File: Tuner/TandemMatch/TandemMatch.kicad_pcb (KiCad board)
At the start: 2 copper layers, 100 x 100 mm, 104 parts, among them J1 Conn_01x02, J10 Conn_01x01, J11 Conn_01x01, J12 Conn_01x01, J13 Conn_01x01, J14 Conn_01x01, J15 Conn_01x01, J16 Conn_01x01, J17 Conn_01x02, J18 Conn_Coaxial, J19 Conn_01x02, J2 Conn_01x02, J20 Conn_Coaxial, J21 Conn_01x01, J22 Conn_01x01, J23 Conn_01x01, J24 Conn_01x01, J25 Conn_01x01, J26 Conn_01x01, J27 Conn_01x01, J28 Conn_01x01, J29 Conn_01x01, J3 Conn_Coaxial, J30 Conn_01x01, J31 Conn_01x01, J32 Conn_01x01, J33 Conn_01x03, J34 Conn_01x01, J35 Conn_01x01, J36 Conn_01x01, J37 Conn_01x01, J38 Conn_01x01, J39 Conn_01x01, J4 Conn_Coaxial, J40 Conn_01x01, J41 Conn_01x01, J42 Conn_Coaxial, J43 Conn_Coaxial, J44 Conn_01x01, J45 Conn_01x01, J46 Conn_01x01, J47 Conn_01x01, J48 Conn_01x01, J49 Conn_01x01, J5 Conn_01x01, J50 Conn_01x01, J51 Conn_01x01, J52 Conn_01x01, J53 Conn_01x01, J54 Conn_01x01, J55 Conn_01x01, J56 Conn_01x01, J57 Conn_01x01, J58 Conn_01x01, J59 Conn_01x01, J6 Conn_01x01, J60 Conn_Coaxial, J61 Conn_Coaxial, J62 Conn_01x04, J63 Conn_01x01, J64 Conn_01x01, J65 Conn_01x01, J66 Conn_01x01, J7 Conn_01x01, J8 Conn_01x01, J9 Conn_01x01

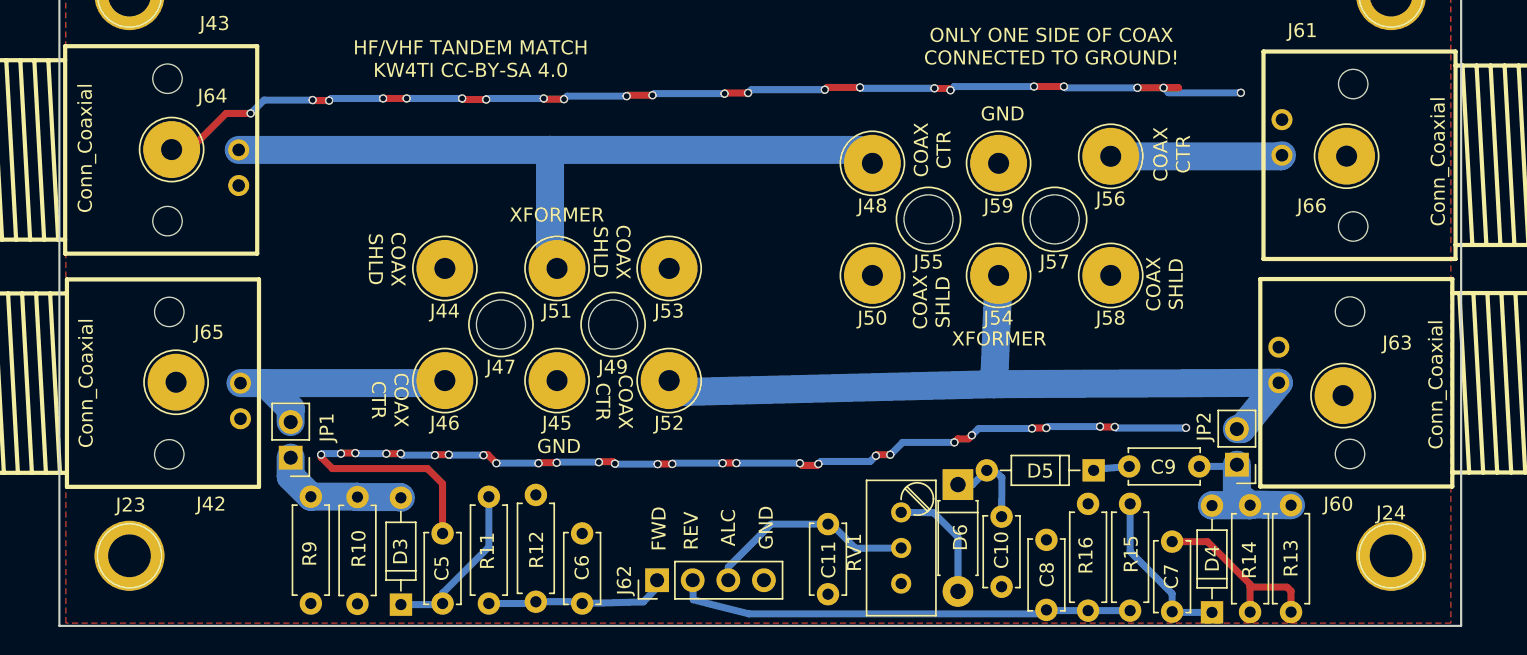
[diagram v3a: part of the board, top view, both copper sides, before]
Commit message: Added Quad Coupler
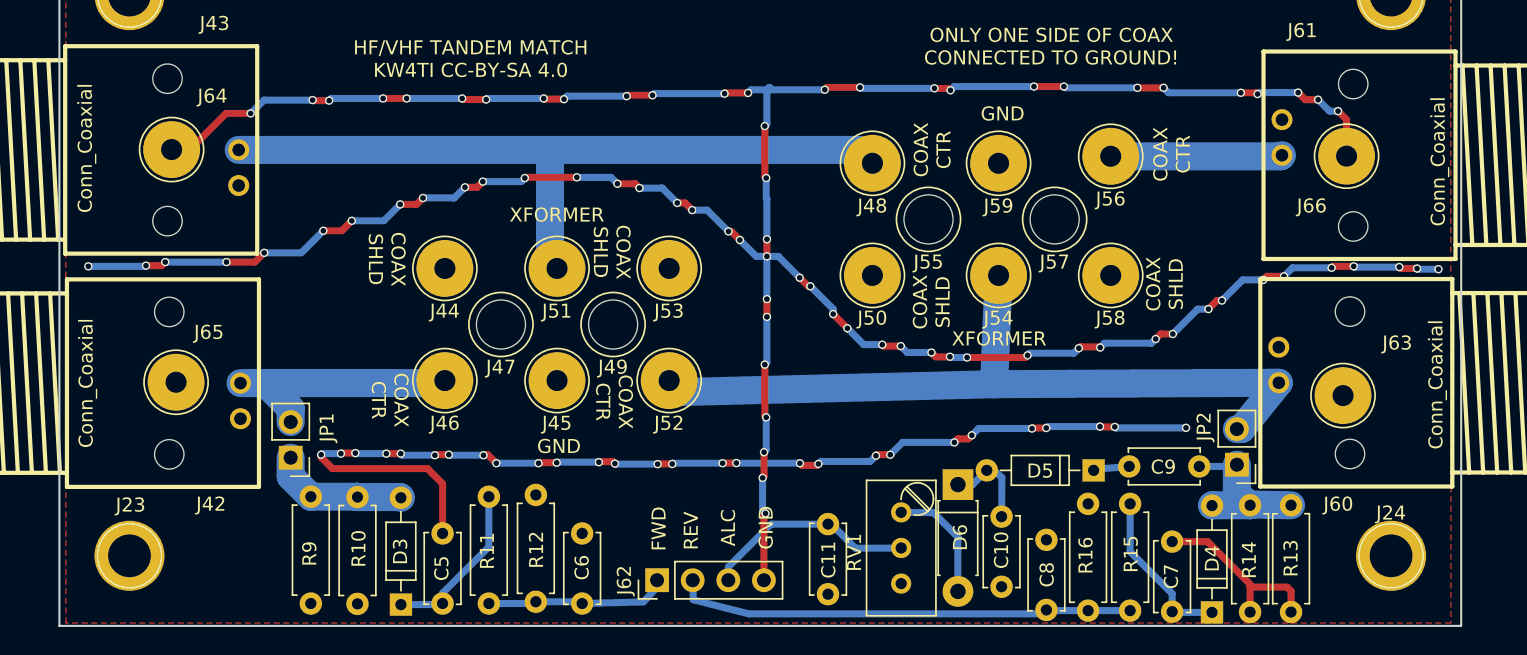
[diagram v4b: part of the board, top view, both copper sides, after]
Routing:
- net GND: track 254.5 -> 406.6 mm, vias 73 -> 130

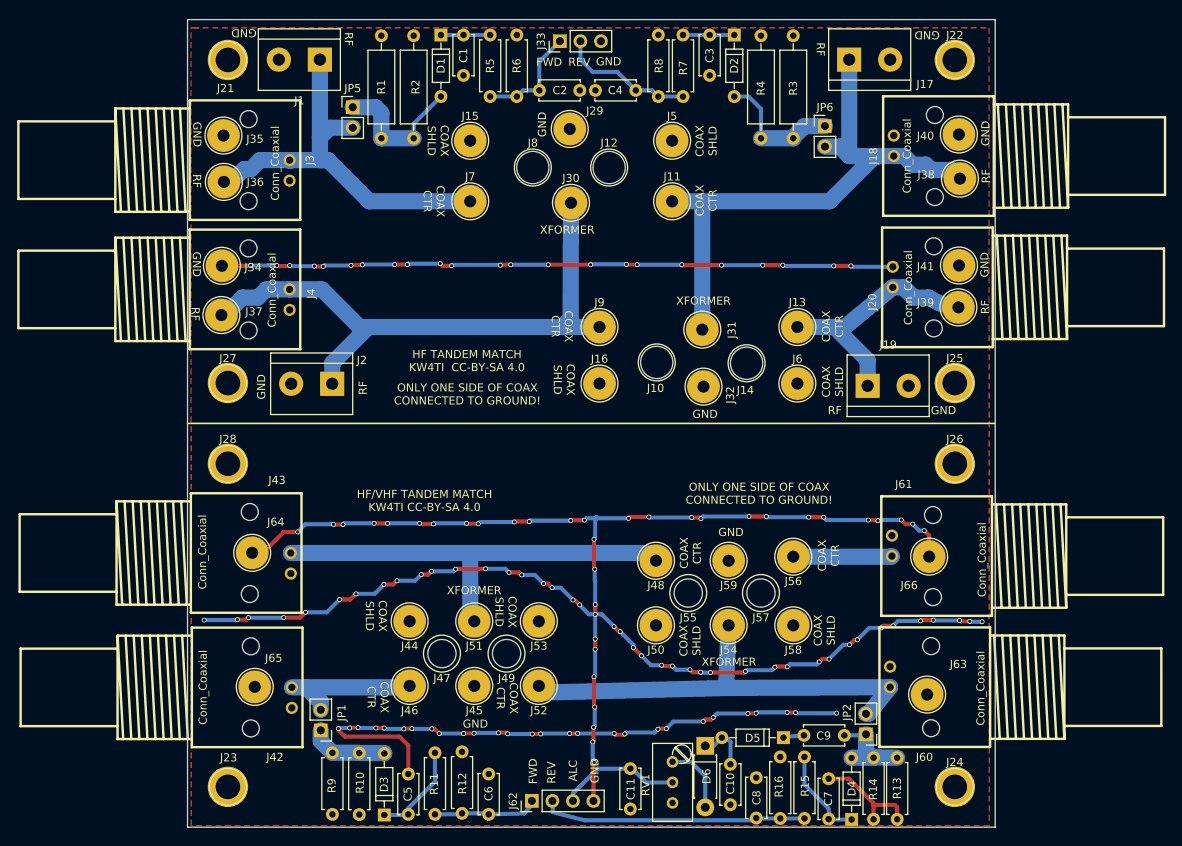
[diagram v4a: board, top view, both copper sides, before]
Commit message: Added more instrumentation to TandemMatch, fixed grounding issue
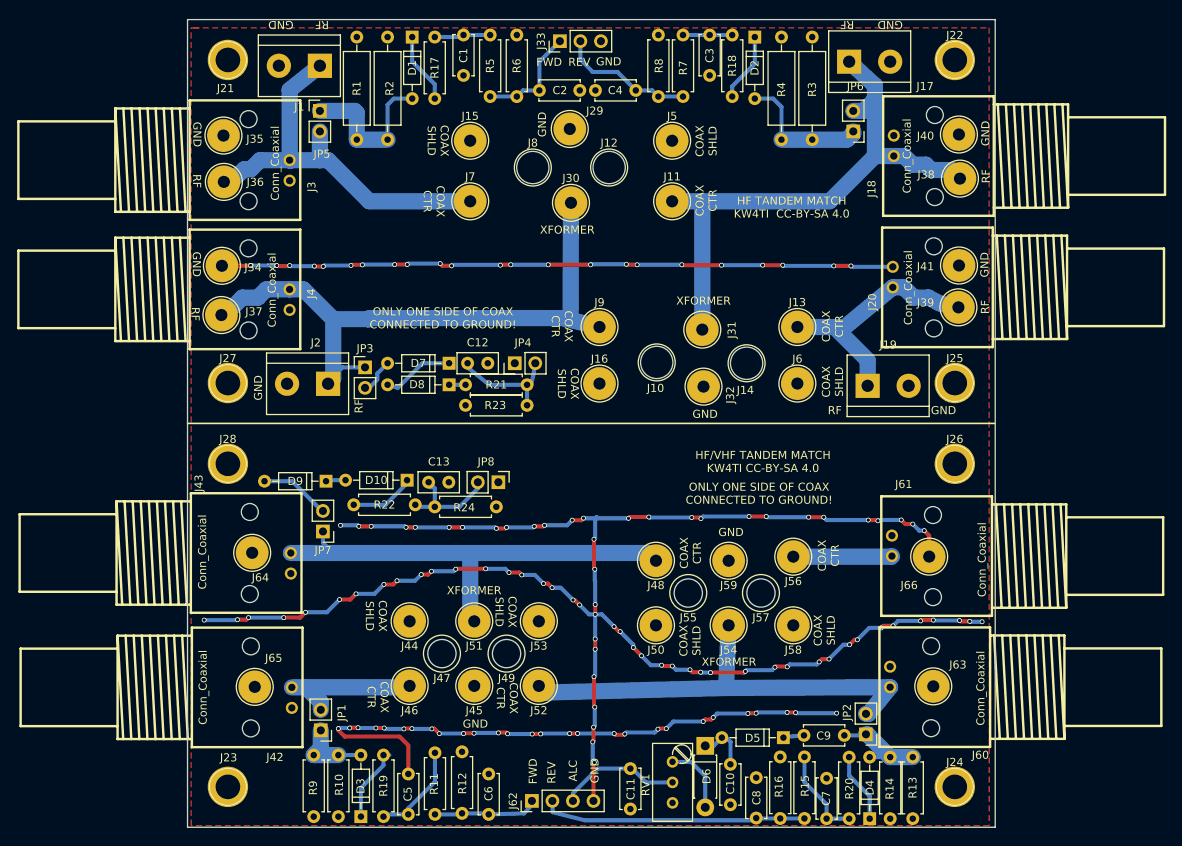
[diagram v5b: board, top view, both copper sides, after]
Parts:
- added C12: 10 nF, Capacitors_THT:C_Disc_D5.0mm_W2.5mm_P2.50mm, F.Cu at (74.7, 82.5)
- added C13: 10 nF, Capacitors_THT:C_Disc_D5.0mm_W2.5mm_P2.50mm, F.Cu at (69.8, 97.3)
- added D10: 1N4148, Diodes_THT:D_DO-35_SOD27_P7.62mm_Horizontal, F.Cu at (67.2, 97.0)
- added D7: 1N4148, Diodes_THT:D_DO-35_SOD27_P7.62mm_Horizontal, F.Cu at (72.4, 82.5)
- added D8: 1N4148, Diodes_THT:D_DO-35_SOD27_P7.62mm_Horizontal, F.Cu at (72.4, 85.2)
- added D9: 1N4148, Diodes_THT:D_DO-35_SOD27_P7.62mm_Horizontal, F.Cu at (57.1, 97.2)
- added JP3: Jumper_NC_Small, Pin_Headers:Pin_Header_Straight_1x02_Pitch2.54mm, F.Cu at (62.0, 83.1)
- added JP4: Jumper_NC_Small, Pin_Headers:Pin_Header_Straight_1x02_Pitch2.54mm, F.Cu at (80.5, 82.5)
- added JP7: Jumper_NC_Small, Pin_Headers:Pin_Header_Straight_1x02_Pitch2.54mm, F.Cu at (56.8, 103.4)
- added JP8: Jumper_NC_Small, Pin_Headers:Pin_Header_Straight_1x02_Pitch2.54mm, F.Cu at (78.5, 97.3)
- added R17: 1k, Resistors_THT:R_Axial_DIN0207_L6.3mm_D2.5mm_P7.62mm_Horizontal, F.Cu at (70.6, 42.2)
- added R18: 1k, Resistors_THT:R_Axial_DIN0207_L6.3mm_D2.5mm_P7.62mm_Horizontal, F.Cu at (107.4, 41.9)
- added R19: 1k, Resistors_THT:R_Axial_DIN0207_L6.3mm_D2.5mm_P7.62mm_Horizontal, F.Cu at (64.3, 138.7)
- added R20: 1k, Resistors_THT:R_Axial_DIN0207_L6.3mm_D2.5mm_P7.62mm_Horizontal, F.Cu at (121.9, 138.9)
- added R21: 1k, Resistors_THT:R_Axial_DIN0207_L6.3mm_D2.5mm_P7.62mm_Horizontal, F.Cu at (82.0, 85.2)
- added R22: 1k, Resistors_THT:R_Axial_DIN0207_L6.3mm_D2.5mm_P7.62mm_Horizontal, F.Cu at (68.2, 100.1)
- added R23: 1k, Resistors_THT:R_Axial_DIN0207_L6.3mm_D2.5mm_P7.62mm_Horizontal, F.Cu at (74.4, 87.8)
- added R24: 1k, Resistors_THT:R_Axial_DIN0207_L6.3mm_D2.5mm_P7.62mm_Horizontal, F.Cu at (78.2, 100.3)
- R11, R12, R15, R16, R5, R6, R7, R8: value 1k -> 10k
- moved JP5 4.09 mm to (56.4, 51.3)
- moved JP6 3.57 mm to (122.4, 53.8), turned to 180 degrees
- moved D1 3.57 mm to (67.8, 42.2)
- moved R2 3.23 mm to (64.8, 42.2)
- moved R1 3.04 mm to (61.0, 42.2)
- moved D3 2.90 mm to (61.5, 138.7)
- moved R10 2.60 mm to (58.7, 138.7)
- moved D2 2.55 mm to (110.2, 42.2)
- moved R4 2.54 mm to (113.5, 42.2)
- moved R3 2.35 mm to (117.3, 42.2)
- moved R9 2.33 mm to (55.6, 138.7)
- moved D4 2.24 mm to (124.5, 138.9)
- moved R14 2.06 mm to (127.0, 138.9)
- moved R13 1.93 mm to (129.8, 138.9)
- moved J63 1.27 mm to (132.3, 122.6)
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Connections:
- D1 pad 1: Net-(C1-Pad1) -> Net-(D1-Pad1)
- D2 pad 1: Net-(C3-Pad1) -> Net-(D2-Pad1)
- D3 pad 1: Net-(C5-Pad1) -> Net-(D3-Pad1)
- D4 pad 1: Net-(C7-Pad1) -> Net-(D4-Pad1)
- J33 pad 3: (no net) -> GND
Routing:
- net GND: track 406.6 -> 382.6 mm
- net Net-(C12-Pad1): track 0.00 -> 14.4 mm
- net Net-(C13-Pad1): track 0.00 -> 13.2 mm
- net Net-(D3-Pad1): track 0.00 -> 9.51 mm
- net Net-(D7-Pad1): track 0.00 -> 8.94 mm
- net Net-(D1-Pad1): track 0.00 -> 8.78 mm
- net Net-(D9-Pad2): track 0.00 -> 8.76 mm
- net Net-(D4-Pad1): track 0.00 -> 8.67 mm
- net Net-(D2-Pad1): track 0.00 -> 8.52 mm
- net Net-(D10-Pad1): track 0.00 -> 8.09 mm
- net Net-(D7-Pad2): track 0.00 -> 5.26 mm
- net Net-(J2-Pad1): track 74.8 -> 78.9 mm
- net Net-(J43-Pad1): track 54.3 -> 57.5 mm
- net Net-(D10-Pad2): track 0.00 -> 2.47 mm
- net Net-(J11-Pad1): track 74.1 -> 71.7 mm
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
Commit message: Removed 1k resistors, did some more rearranging on TandemMatch
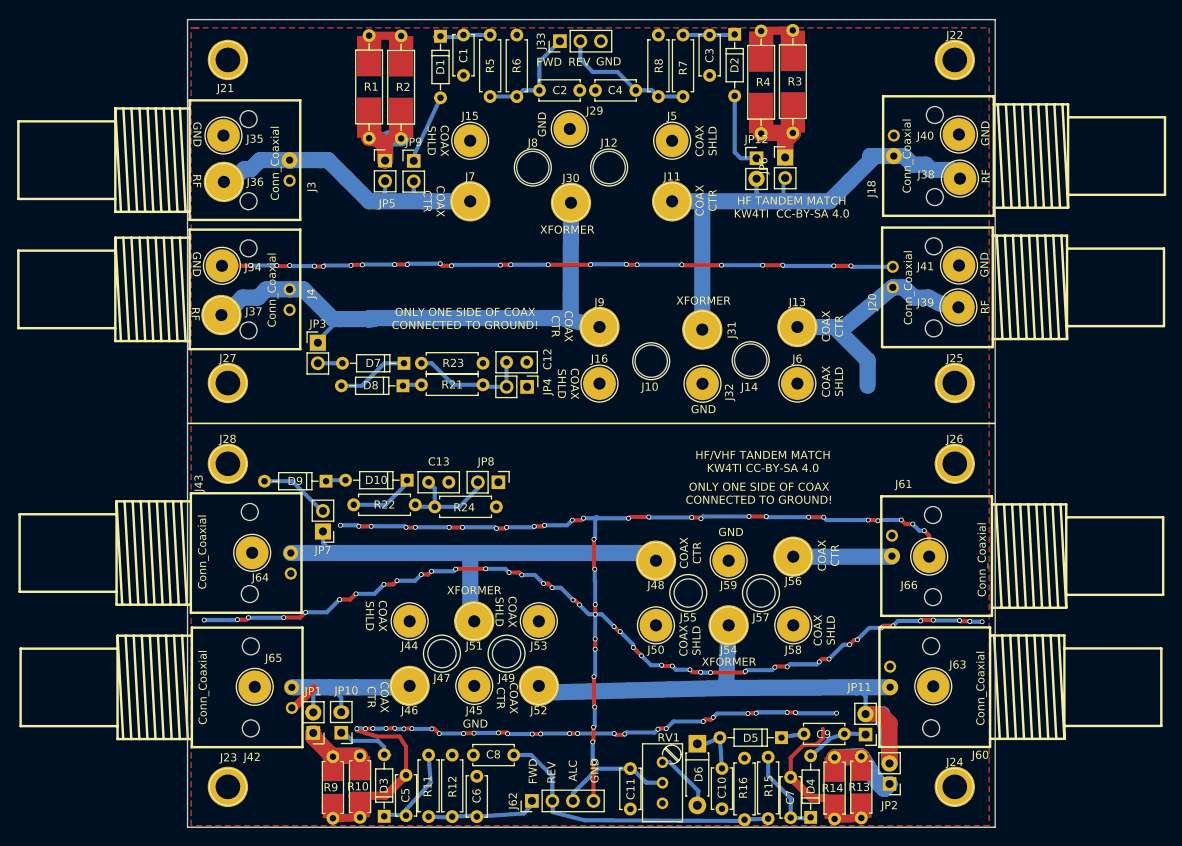
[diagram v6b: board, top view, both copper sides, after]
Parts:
- removed J1, J17, J19, J2: Conn_01x02, Connectors_Terminal_Blocks:TerminalBlock_bornier-2_P5.08mm
- removed R17, R18, R19, R20: 1k, Resistors_THT:R_Axial_DIN0207_L6.3mm_D2.5mm_P7.62mm_Horizontal
- added JP10: Jumper_NC_Small, Pin_Headers:Pin_Header_Straight_1x02_Pitch2.54mm, F.Cu at (59.0, 128.3)
- added JP11: Jumper_NC_Small, Pin_Headers:Pin_Header_Straight_1x02_Pitch2.54mm, F.Cu at (124.0, 128.5)
- added JP12: Jumper_NC_Small, Pin_Headers:Pin_Header_Straight_1x02_Pitch2.54mm, F.Cu at (110.4, 57.2)
- added JP9: Jumper_NC_Small, Pin_Headers:Pin_Header_Straight_1x02_Pitch2.54mm, F.Cu at (68.0, 57.5)
- R1, R2, R3, R4: footprint Resistors_THT:R_Axial_DIN0309_L9.0mm_D3.2mm_P12.70mm_Horizontal -> TandemMatch:R_Axial_DIN0309_L9.0mm_D3.2mm_P12.70mm_Horizontal
- R10, R13, R14, R9: footprint Resistors_THT:R_Axial_DIN0207_L6.3mm_D2.5mm_P7.62mm_Horizontal -> TandemMatch:R_Axial_DIN0207_L6.3mm_D2.5mm_P7.62mm_Horizontal_SMD
- R21, R22: value 1k -> 10k
- moved C8 31.0 mm to (80.4, 131.1), turned to 180 degrees
- moved JP5 10.2 mm to (64.5, 57.5)
- moved JP6 9.03 mm to (114.0, 57.1), turned to 0 degrees
- moved D4 7.31 mm to (117.2, 138.8)
- moved R14 6.89 mm to (120.1, 139.0)
- moved JP2 6.80 mm to (126.9, 134.6)
- moved JP3 6.59 mm to (56.1, 80.0)
- moved R13 6.37 mm to (123.4, 138.8)
- moved D8 5.72 mm to (66.7, 85.3)
- moved R23 5.64 mm to (76.6, 82.5), turned to 180 degrees
- moved D7 5.59 mm to (66.8, 82.5)
- moved R21 5.46 mm to (76.6, 85.2)
- moved C12 4.83 mm to (79.5, 82.4)
- moved R15 4.50 mm to (111.9, 138.9)
- moved C7 4.45 mm to (114.7, 138.8)
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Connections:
- D1 pad 1: Net-(D1-Pad1) -> Net-(C1-Pad1)
- D2 pad 1: Net-(D2-Pad1) -> Net-(C3-Pad1)
- D3 pad 1: Net-(D3-Pad1) -> Net-(C5-Pad1)
- D4 pad 1: Net-(D4-Pad1) -> Net-(C7-Pad1)
- JP1 pad 1: Net-(D3-Pad2) -> Net-(JP1-Pad1)
- JP2 pad 1: Net-(C9-Pad2) -> Net-(JP2-Pad1)
- JP5 pad 1: Net-(D1-Pad2) -> Net-(JP5-Pad1)
- JP6 pad 1: Net-(D2-Pad2) -> Net-(JP6-Pad1)
- R1 pad 2: Net-(D1-Pad2) -> Net-(JP5-Pad1)
- R10 pad 2: Net-(D3-Pad2) -> Net-(JP1-Pad1)
- R13 pad 2: Net-(C9-Pad2) -> Net-(JP2-Pad1)
- R14 pad 2: Net-(C9-Pad2) -> Net-(JP2-Pad1)
- R2 pad 2: Net-(D1-Pad2) -> Net-(JP5-Pad1)
- R3 pad 2: Net-(D2-Pad2) -> Net-(JP6-Pad1)
- R4 pad 2: Net-(D2-Pad2) -> Net-(JP6-Pad1)
- R9 pad 2: Net-(D3-Pad2) -> Net-(JP1-Pad1)
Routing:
- net GND: track 382.6 -> 436.8 mm
- net Net-(JP2-Pad1): track 0.00 -> 25.2 mm
- net Net-(JP6-Pad1): track 0.00 -> 24.7 mm
- net Net-(JP1-Pad1): track 0.00 -> 20.8 mm
- net Net-(JP5-Pad1): track 0.00 -> 17.7 mm
- net Net-(J52-Pad1): track 56.2 -> 72.1 mm
- net Net-(J3-Pad1): track 51.4 -> 39.7 mm
- net Net-(D1-Pad2): track 19.5 -> 8.66 mm
- net Net-(D3-Pad1): track 9.51 -> 0.00 mm
- net Net-(D1-Pad1): track 8.78 -> 0.00 mm
- net Net-(D4-Pad1): track 8.67 -> 0.00 mm
- net Net-(D2-Pad1): track 8.52 -> 0.00 mm
- net Net-(J30-Pad1): track 78.9 -> 71.3 mm
- net Net-(D2-Pad2): track 17.2 -> 10.3 mm
- net Net-(J11-Pad1): track 71.7 -> 65.5 mm
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
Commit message: Added BNC and screw terminal combo pads
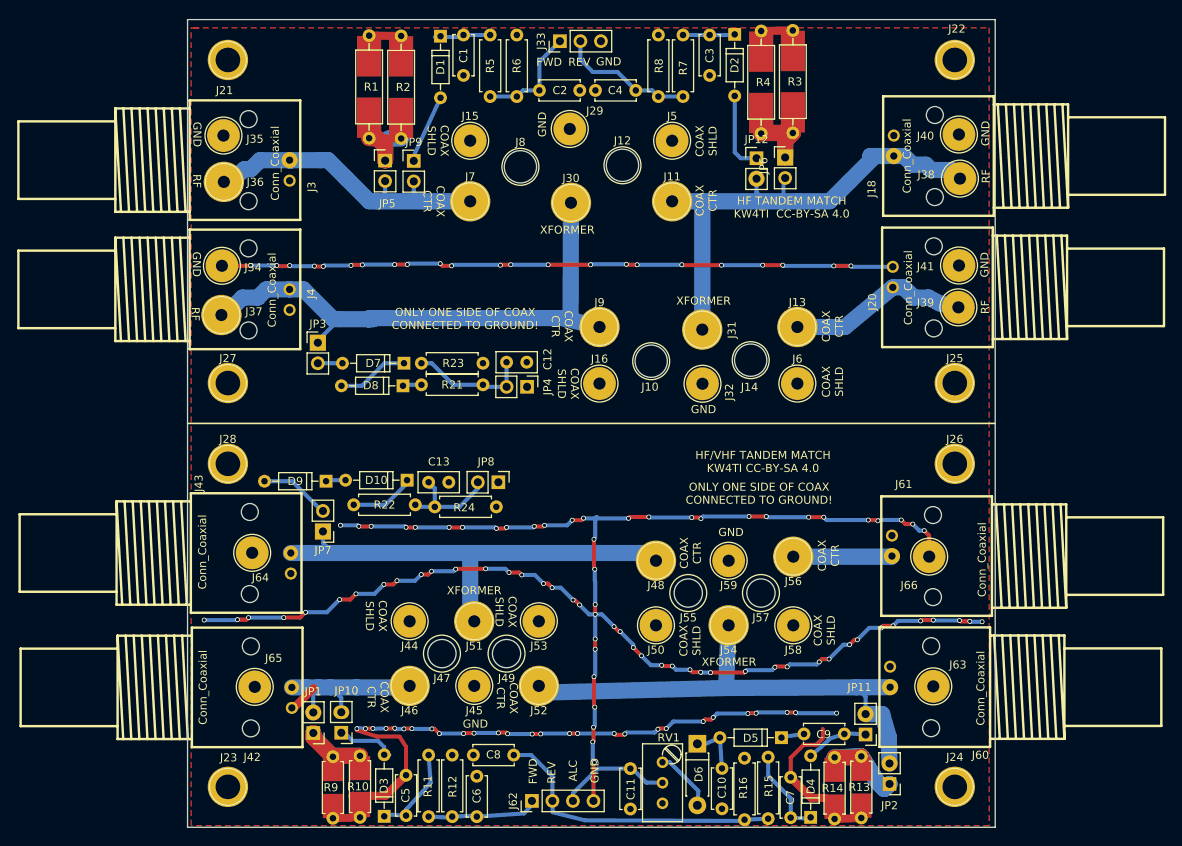
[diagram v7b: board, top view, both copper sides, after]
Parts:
- moved J12 1.67 mm to (93.9, 58.0)
- moved J8 1.54 mm to (81.2, 58.2)
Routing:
- net Net-(J13-Pad1): track 31.4 -> 22.5 mm
- net Net-(J52-Pad1): track 72.1 -> 63.7 mm
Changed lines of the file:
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@@
     (links 159)
     (no_connects 0)
-    (area 18.708999 37.92438 161.377001 141.488519)
+    (area 39.924999 39.924999 140.075001 140.075001)
     (thickness 1.6)
     (drawings 49)
-    (tracks 686)
+    (tracks 681)
     (zones 0)
     (modules 118)
@@
   )
   (setup
-    (last_trace_width 0.5)
+    (last_trace_width 0.25)
     (user_trace_width 0.35)
     (user_trace_width 0.5)
@@
   )
   (module Connectors:1pin (layer F.Cu)
-    (at 82.7532 58.3184)
+    (at 81.2165 58.2295)
     (descr "module 1 pin (ou trou mecanique de percage)")
     (tags DEV)
@@
   )
   (module Connectors:1pin (layer F.Cu)
-    (at 92.202 58.3184)
+    (at 93.853 58.039)
     (descr "module 1 pin (ou trou mecanique de percage)")
     (tags DEV)
@@
     (descr "module 1 pin (ou trou mecanique de percage)")
     (tags DEV)
-    (fp_text reference J21 (at -0.296 3.514) (layer F.SilkS)
+    (fp_text reference J21 (at -0.423 3.768) (layer F.SilkS)
       (effects (font (size 1 1) (thickness 0.15)))
     )
@@
     (descr "module 1 pin (ou trou mecanique de percage)")
     (tags DEV)
-    (fp_text reference J22 (at 0 -3.048) (layer F.SilkS)
+    (fp_text reference J22 (at 0.255 -3.852) (layer F.SilkS)
       (effects (font (size 1 1) (thickness 0.15)))
     )
@@
     (descr "module 1 pin (ou trou mecanique de percage)")
     (tags DEV)
-    (fp_text reference J24 (at 0 -3.048) (layer F.SilkS)
+    (fp_text reference J24 (at 0.001 -3.682) (layer F.SilkS)
       (effects (font (size 1 1) (thickness 0.15)))
     )
@@
   (segment (start 120.101 78.064) (end 121.392 78.064) (width 2) (layer B.Cu) (net 3))
   (segment (start 121.392 78.064) (end 127.32 73.152) (width 2) (layer B.Cu) (net 3) (status 20))
-  (segment (start 124.206 85.344) (end 124.206 82.169) (width 2) (layer B.Cu) (net 3) (status 10))
-  (segment (start 124.206 82.169) (end 120.101 78.064) (width 2) (layer B.Cu) (net 3))
   (segment (start 115.508 78.064) (end 120.101 78.064) (width 2) (layer B.Cu) (net 3) (status 10))
   (segment (start 77.47 41.91) (end 74.168 41.91) (width 0.5) (layer B.Cu) (net 4))
@@
   (segment (start 75 106.045) (end 97.045 106.045) (width 2) (layer B.Cu) (net 10))
   (segment (start 97.045 106.045) (end 98 107) (width 2) (layer B.Cu) (net 10))
-  (segment (start 123.952 125.984) (end 125.7935 125.984) (width 2) (layer F.Cu) (net 11))
-  (segment (start 125.7935 125.984) (end 126.91872 127.10922) (width 2) (layer F.Cu) (net 11))
-  (segment (start 126.91872 127.10922) (end 126.91872 132.10032) (width 2) (layer F.Cu) (net 11))
   (segment (start 123.952 125.984) (end 126.0094 125.984) (width 2) (layer B.Cu) (net 11))
   (segment (start 126.81712 128.80848) (end 126.91872 132.10032) (width 2) (layer B.Cu) (net 11) (status 20))
